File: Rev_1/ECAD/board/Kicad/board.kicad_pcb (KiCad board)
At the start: 4 copper layers, 122 parts, among them Q200 PMOS, Q201 PNP, Q202 PNP, SW300 6x6, SW301 6x6, SW302 6x6, SW303 6x6, U1 SD_CARD_READER, U100 ATMega328P-AU, U101 ICSP, U2 LCD OLED, U200 USB_C_6PIN, U202 FT232RL, U203 L7805ABV, U301 74HC245, U302 74HC245, U303 74HC595, U304 74HC595, U305 74HC595, U306 AT28C64B-15PU, U307 Summer, Y100 16MHZ

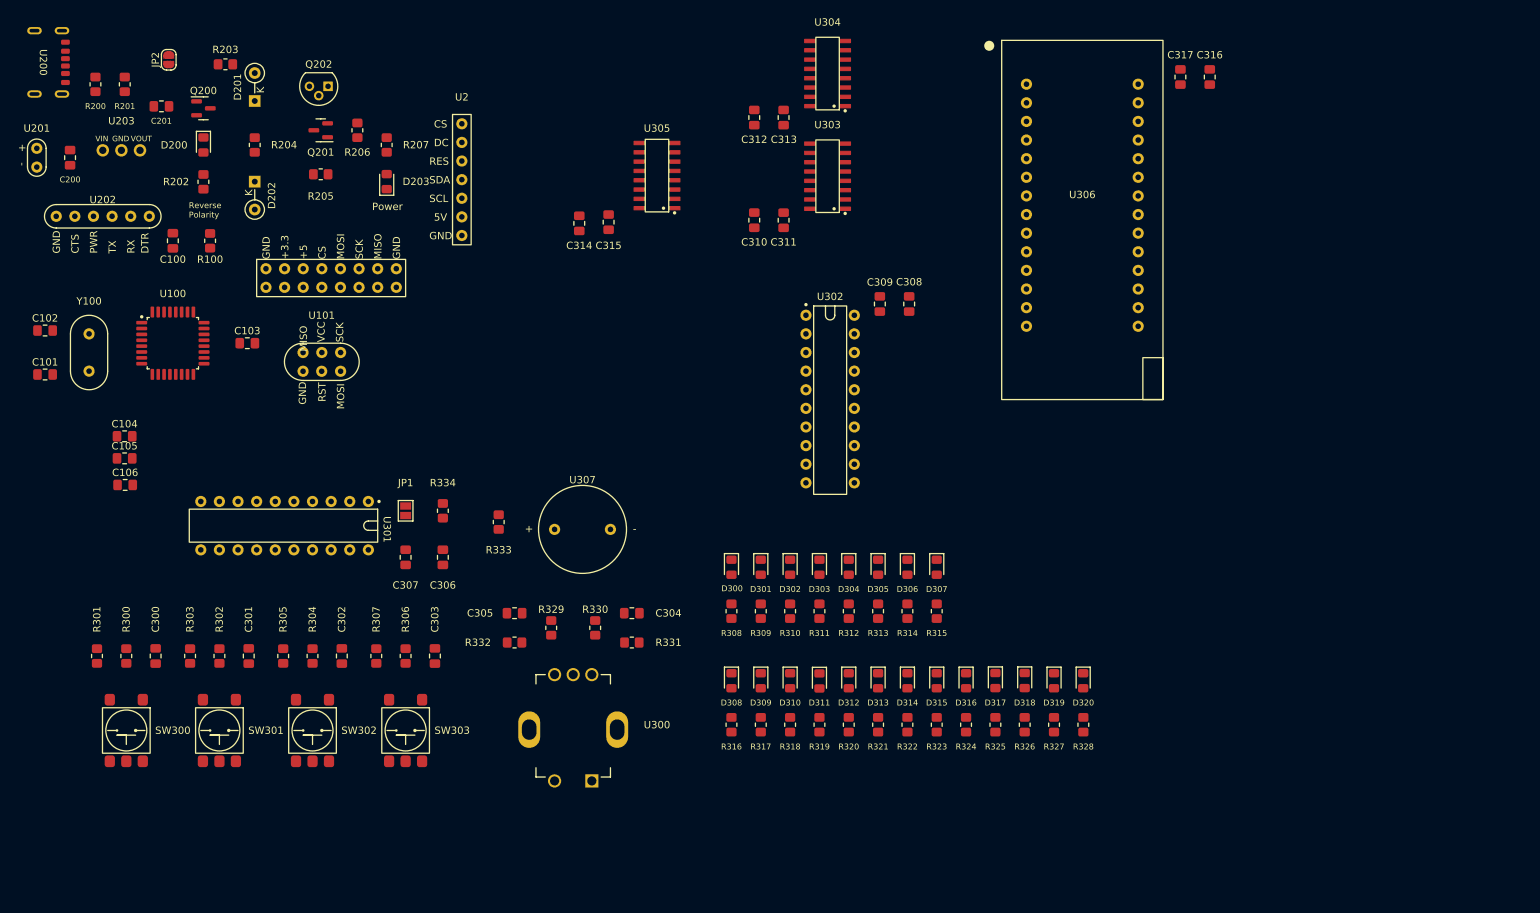
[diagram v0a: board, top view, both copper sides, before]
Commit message: Added cutout to the pcb
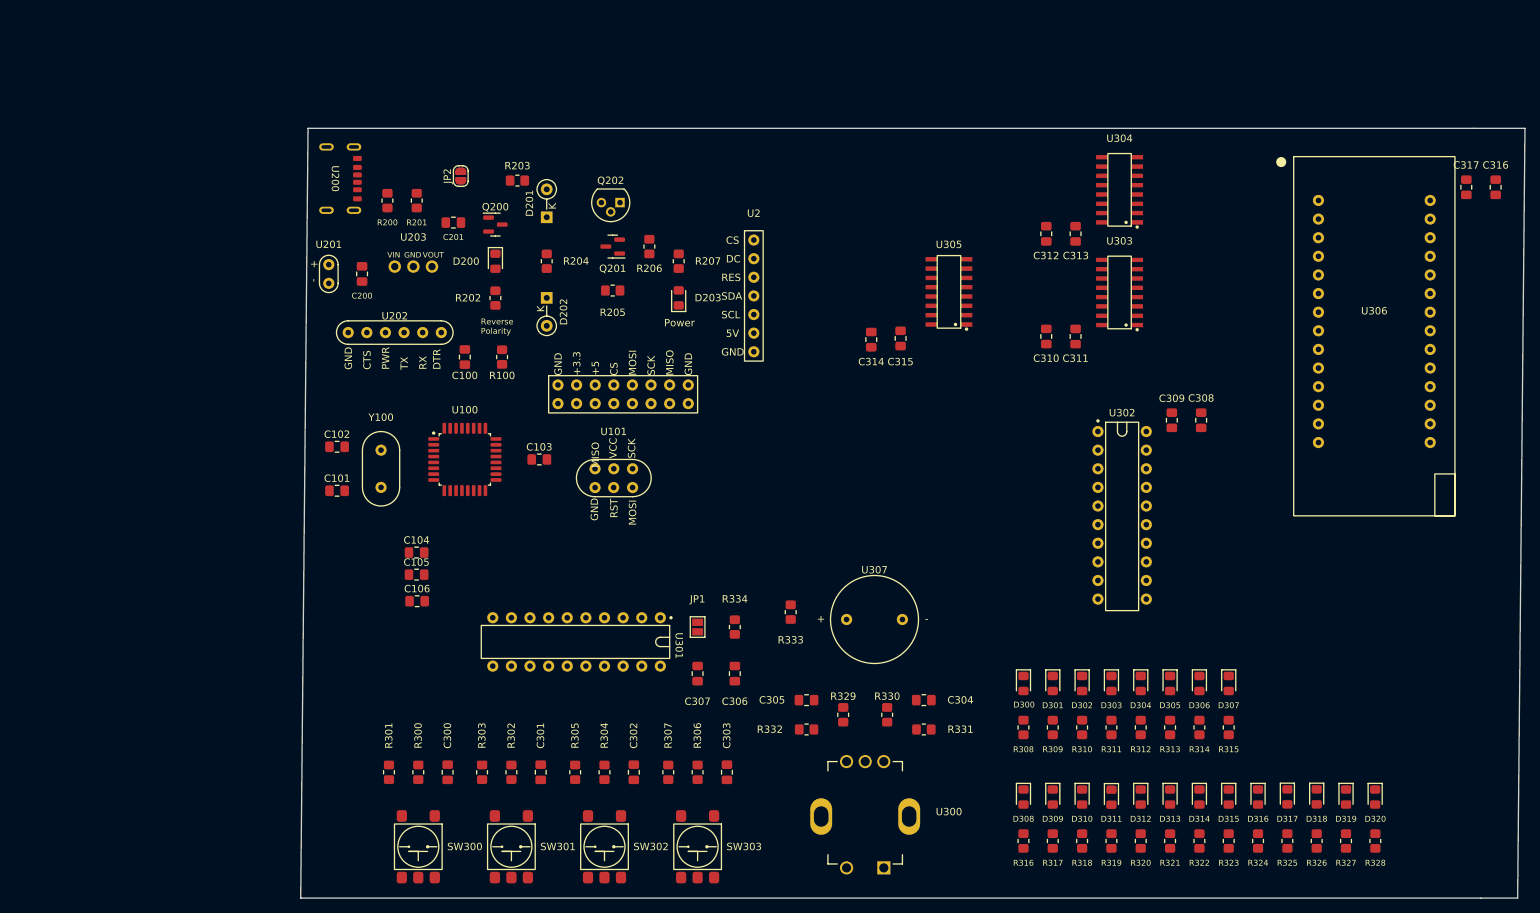
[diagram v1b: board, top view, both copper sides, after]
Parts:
- moved C308 42.9 mm to (175.8, 77.8)
- moved C309 42.9 mm to (171.8, 77.8)
- moved C314 42.9 mm to (130.8, 66.8)
- moved C315 42.9 mm to (134.8, 66.7)
- moved D305 42.9 mm to (171.6, 113.7)
- moved D306 42.9 mm to (175.6, 113.7)
- moved D307 42.9 mm to (179.6, 113.7)
- moved D313 42.9 mm to (171.6, 129.2)
- moved D314 42.9 mm to (175.6, 129.2)
- moved D315 42.9 mm to (179.6, 129.2)
- moved D316 42.9 mm to (183.6, 129.2)
- moved D317 42.9 mm to (187.6, 129.2)
- moved D318 42.9 mm to (191.6, 129.2)
- moved D319 42.9 mm to (195.6, 129.2)
- moved R203 42.9 mm to (82.6, 45.1)
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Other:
- board outline added: 167 x 105 mm

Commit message: Most of the GND vias are in place and the power section is mostly done
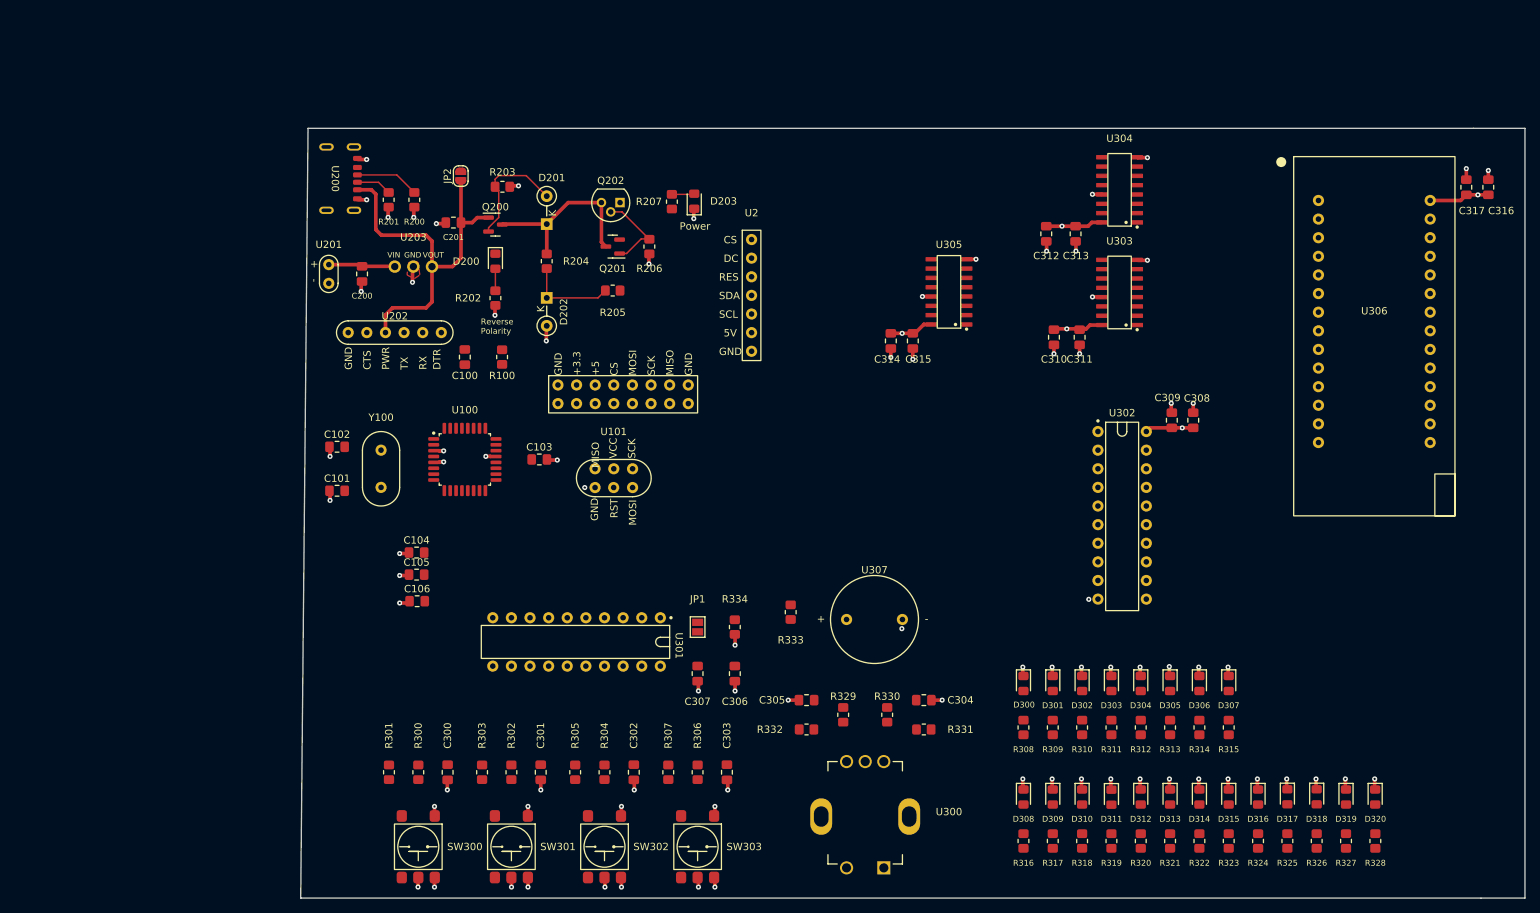
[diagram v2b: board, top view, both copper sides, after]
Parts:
- moved D203 13.4 mm to (106.7, 47.9)
- moved R207 8.18 mm to (103.6, 48.0)
- moved R201 3.83 mm to (65.0, 47.8)
- moved R200 3.67 mm to (68.5, 47.8)
- moved C314 2.68 mm to (133.5, 67.0)
- moved R203 2.21 mm to (80.5, 46.0)
- moved C315 1.70 mm to (136.5, 67.0)
- moved C308 1.08 mm to (174.8, 77.8)
- moved C310 1.06 mm to (155.8, 66.5)
- moved C316 1.00 mm to (215.0, 46.0)
- moved D201 0.93 mm to (86.6, 51.1)
- moved C311 0.56 mm to (159.2, 66.5)
- moved U2 0.32 mm to (114.5, 60.8)
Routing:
- net GND: track 0.00 -> 98.4 mm, vias 0 -> 82
- net /Voltage Input/5V_REGULATED: track 0.00 -> 52.7 mm
- net +5V: track 0.00 -> 35.2 mm, vias 0 -> 5
- net /Voltage Input/POLARITY_PROTECTED: track 0.00 -> 25.1 mm
- net /Voltage Input/VGS: track 0.00 -> 16.3 mm
- net Net-(D202-K): track 0.00 -> 12.4 mm
- net Net-(Q201-C): track 0.00 -> 11.7 mm
- net /Voltage Input/BATTERY_INPUT: track 0.00 -> 9.11 mm
- net /Voltage Input/USB_CC1: track 0.00 -> 8.75 mm
- net /Voltage Input/USB_CC2: track 0.00 -> 4.84 mm
- net Net-(D203-A): track 0.00 -> 3.08 mm
- net Net-(D200-A): track 0.00 -> 3.00 mm
- added copper zone on F.Cu, net GND
- added copper zone on In1.Cu, net GND
- added copper zone on In2.Cu, net GND
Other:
- outline, holes or cut-outs redrawn
